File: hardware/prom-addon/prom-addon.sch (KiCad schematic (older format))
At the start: 5 parts

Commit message: The ROM reader addon schematic finished.
We are pretty much ready for layout. Status as of @esden twitch stream
on 2020-09-01.
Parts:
- removed U? (x2): 74HC164, symbol 74xx:74HC164
- added JP1, JP2: Pin Mode, Connector_PinHeader_2.54mm:PinHeader_1x03_P2.54mm_Vertical, symbol Jumper:Jumper_3_Bridged12
- added RN1, RN2, RN3: 100R, Resistor_SMD:R_Array_Convex_4x0402, symbol Device:R_Pack04
- added U1, U2: 74HC595, pkl_housings_dfn_qfn:DHVQFN-16_2.5x3.5mm_Pitch0.5mm, symbol 74xx:74HC595
- J1, J2: renamed from J?; footprint (none) -> Connector_PinSocket_2.54mm:PinSocket_2x10_P2.54mm_Vertical
- gave numbers to parts that had none: 1
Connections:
- net labels added: A_LATCH, A_SI´, P1, P27, ~OE
- wire segments 116 -> 137
- no-connect marks 10 -> 9
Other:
- note added: "Can be\nVpp or A15"
- note added: "Can be\n~PGM~ or A14"
- note added: "TODO:"
- note removed: "TODO:\n* Figure out if A15/PGM/VPP need jumpers\n* Figure out if the sift registers need to be different\n* Jumpering/padding for CE vs Address lines"
- moved on the sheet: J1, J2, U3

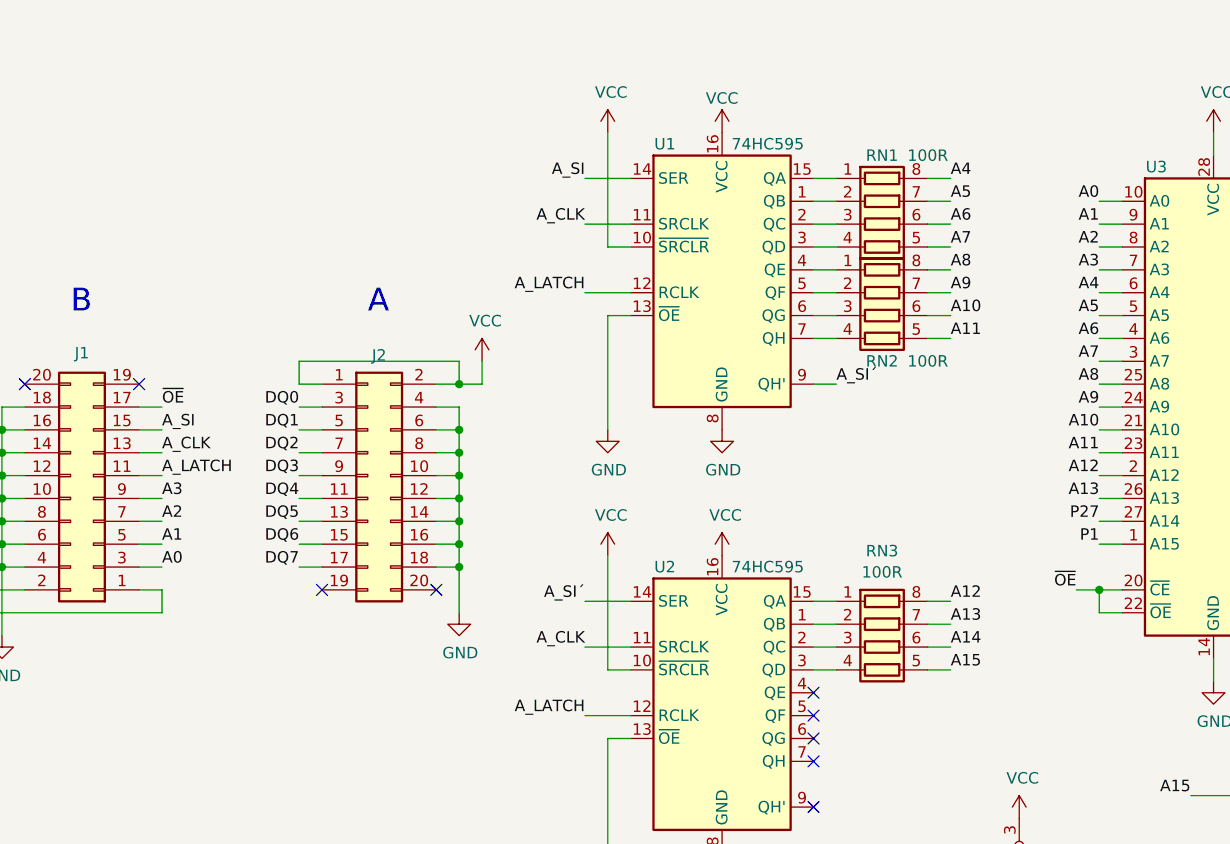
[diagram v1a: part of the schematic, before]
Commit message: prom: Routed the first version of the board.
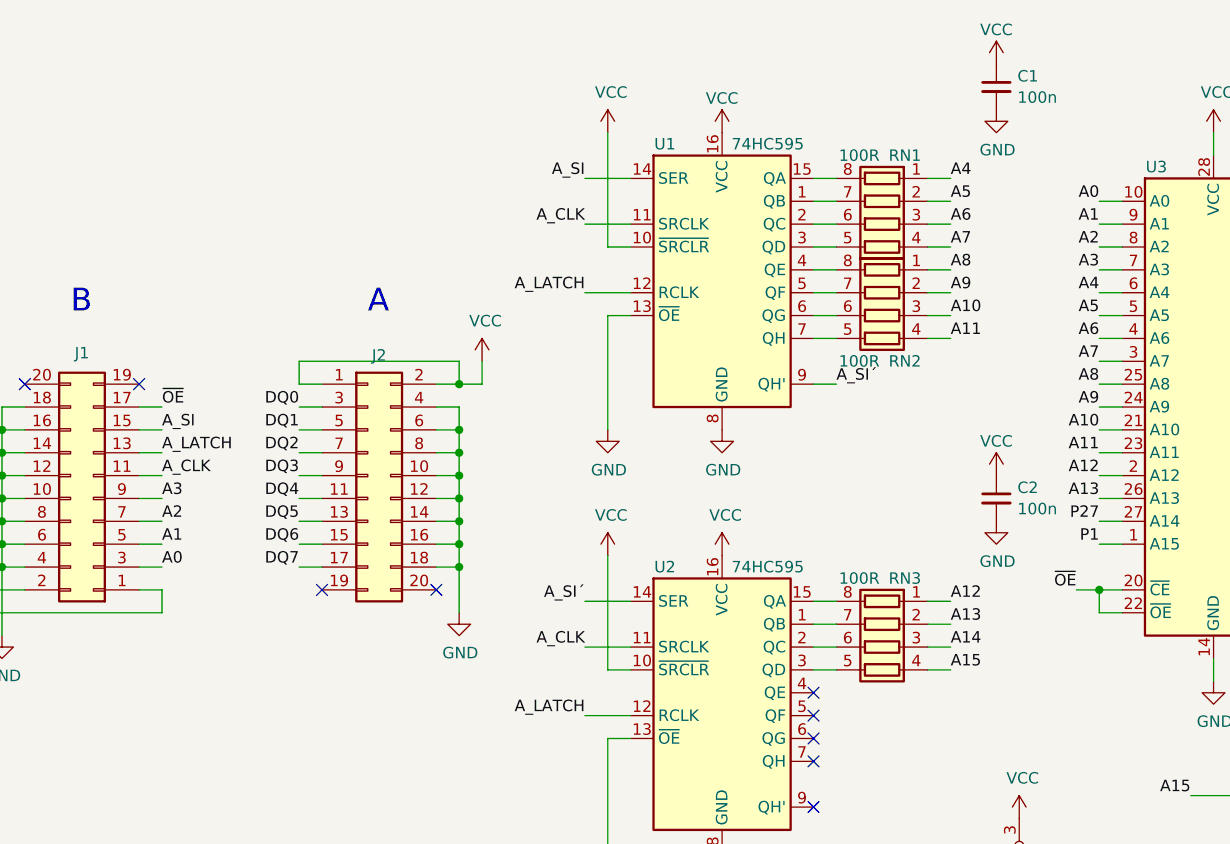
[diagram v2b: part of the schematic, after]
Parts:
- added C1, C2: 100n, pkl_dipol:C_0402, symbol Device:C_Small
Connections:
- net A10: now also RN2.3 (R3.1); no longer RN2.6 (R3.2)
- net A11: now also RN2.4 (R4.1); no longer RN2.5 (R4.2)
- net A12: now also RN3.1 (R1.1); no longer RN3.8 (R1.2)
- net A13: now also RN3.2 (R2.1); no longer RN3.7 (R2.2)
- net A14: now also RN3.3 (R3.1); no longer RN3.6 (R3.2)
- net A15: now also RN3.4 (R4.1); no longer RN3.5 (R4.2)
- net A4: now also RN1.1 (R1.1); no longer RN1.8 (R1.2)
- net A5: now also RN1.2 (R2.1); no longer RN1.7 (R2.2)
- net A6: now also RN1.3 (R3.1); no longer RN1.6 (R3.2)
- net A7: now also RN1.4 (R4.1); no longer RN1.5 (R4.2)
- net A8: now also RN2.1 (R1.1); no longer RN2.8 (R1.2)
- net A9: now also RN2.2 (R2.1); no longer RN2.7 (R2.2)
- net A_CLK: now also J1.11 (Pin_11); no longer J1.13 (Pin_13)
- net A_LATCH: now also J1.13 (Pin_13); no longer J1.11 (Pin_11)
- net GND: now also C1.2, C2.2
- net VCC: now also C1.1, C2.1
- net at U1.15 (QA): now also RN1.8 (R1.2); no longer RN1.1 (R1.1)
- net at U1.1 (QB): now also RN1.7 (R2.2); no longer RN1.2 (R2.1)
- net at U1.2 (QC): now also RN1.6 (R3.2); no longer RN1.3 (R3.1)
- net at U1.3 (QD): now also RN1.5 (R4.2); no longer RN1.4 (R4.1)
- net at U1.4 (QE): now also RN2.8 (R1.2); no longer RN2.1 (R1.1)
- net at U1.5 (QF): now also RN2.7 (R2.2); no longer RN2.2 (R2.1)
- net at U1.6 (QG): now also RN2.6 (R3.2); no longer RN2.3 (R3.1)
- net at U1.7 (QH): now also RN2.5 (R4.2); no longer RN2.4 (R4.1)
- net at U2.15 (QA): now also RN3.8 (R1.2); no longer RN3.1 (R1.1)
- net at U2.1 (QB): now also RN3.7 (R2.2); no longer RN3.2 (R2.1)
- net at U2.2 (QC): now also RN3.6 (R3.2); no longer RN3.3 (R3.1)
- net at U2.3 (QD): now also RN3.5 (R4.2); no longer RN3.4 (R4.1)
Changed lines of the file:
@@
 Text Label 2500 2300 0    50   ~ 0
 A_SI
-Text Label 2500 2400 0    50   ~ 0
+Text Label 2500 2500 0    50   ~ 0
 A_CLK
 Text Label 2500 2900 0    50   ~ 0
@@
 	6600 3000 6500 3000
 Connection ~ 6600 3000
-Text Label 2500 2500 0    50   ~ 0
+Text Label 2500 2400 0    50   ~ 0
 A_LATCH
 Text Label 2500 2200 0    50   ~ 0
@@
 U 1 1 5F57774C
 P 5650 1400
-F 0 "RN1" V 5350 1400 50  0000 C CNN
-F 1 "100R" V 5350 1600 50  0000 C CNN
+F 0 "RN1" V 5350 1300 50  0000 C CNN
+F 1 "100R" V 5350 1500 50  0000 C CNN
 F 2 "Resistor_SMD:R_Array_Convex_4x0402" V 5925 1400 50  0001 C CNN
 F 3 "~" H 5650 1400 50  0001 C CNN
 	1    5650 1400
-	0    1    1    0
+	0    -1   1    0
 $EndComp
 $Comp
@@
 U 1 1 5F581391
 P 5650 1800
-F 0 "RN2" V 5850 1800 50  0000 C CNN
-F 1 "100R" V 5850 2000 50  0000 C CNN
+F 0 "RN2" V 5850 1700 50  0000 C CNN
+F 1 "100R" V 5850 1900 50  0000 C CNN
 F 2 "Resistor_SMD:R_Array_Convex_4x0402" V 5925 1800 50  0001 C CNN
 F 3 "~" H 5650 1800 50  0001 C CNN
 	1    5650 1800
-	0    1    1    0
+	0    -1   1    0
 $EndComp
 Wire Wire Line
@@
 U 1 1 5F5B0FC8
 P 5650 3250
-F 0 "RN3" V 5230 3250 50  0000 C CNN
-F 1 "100R" V 5323 3250 50  0000 C CNN
+F 0 "RN3" V 5350 3150 50  0000 C CNN
+F 1 "100R" V 5350 3350 50  0000 C CNN
 F 2 "Resistor_SMD:R_Array_Convex_4x0402" V 5925 3250 50  0001 C CNN
 F 3 "~" H 5650 3250 50  0001 C CNN
 	1    5650 3250
-	0    1    1    0
+	0    -1   1    0
 $EndComp
 Wire Wire Line
@@
 Wire Wire Line
 	6600 2800 6700 2800
+$Comp
+L Device:C_Small C2
+U 1 1 5F744BFD
+P 6150 2600
+F 0 "C2" H 6242 2647 50  0000 L CNN
+F 1 "100n" H 6242 2554 50  0000 L CNN
+F 2 "pkl_dipol:C_0402" H 6150 2600 50  0001 C CNN
+F 3 "~" H 6150 2600 50  0001 C CNN
+	1    6150 2600
+	1    0    0    -1
+$EndComp
+$Comp
+L Device:C_Small C1
+U 1 1 5F745589
+P 6150 800
+F 0 "C1" H 6242 847 50  0000 L CNN
+F 1 "100n" H 6242 754 50  0000 L CNN
+F 2 "pkl_dipol:C_0402" H 6150 800 50  0001 C CNN
+F 3 "~" H 6150 800 50  0001 C CNN
+	1    6150 800
+	1    0    0    -1
+$EndComp
+$Comp
+L power:GND #PWR0117
+U 1 1 5F745B98
+P 6150 900
+F 0 "#PWR0117" H 6150 650 50  0001 C CNN
+F 1 "GND" H 6155 724 50  0000 C CNN
+F 2 "" H 6150 900 50  0001 C CNN
+F 3 "" H 6150 900 50  0001 C CNN
+	1    6150 900
+	1    0    0    -1
+$EndComp
+$Comp
+L power:VCC #PWR0118
+U 1 1 5F74C028
+P 6150 700
+F 0 "#PWR0118" H 6150 550 50  0001 C CNN
+F 1 "VCC" H 6150 850 50  0000 C CNN
+F 2 "" H 6150 700 50  0001 C CNN
+F 3 "" H 6150 700 50  0001 C CNN
+	1    6150 700
+	1    0    0    -1
+$EndComp
+$Comp
+L power:VCC #PWR0119
+U 1 1 5F759CD8
+P 6150 2500
+F 0 "#PWR0119" H 6150 2350 50  0001 C CNN
+F 1 "VCC" H 6150 2650 50  0000 C CNN
+F 2 "" H 6150 2500 50  0001 C CNN
+F 3 "" H 6150 2500 50  0001 C CNN
+	1    6150 2500
+	1    0    0    -1
+$EndComp
+$Comp
+L power:GND #PWR0120
+U 1 1 5F759F0D
+P 6150 2700
+F 0 "#PWR0120" H 6150 2450 50  0001 C CNN
+F 1 "GND" H 6155 2524 50  0000 C CNN
+F 2 "" H 6150 2700 50  0001 C CNN
+F 3 "" H 6150 2700 50  0001 C CNN
+	1    6150 2700
+	1    0    0    -1
+$EndComp
 $EndSCHEMATC

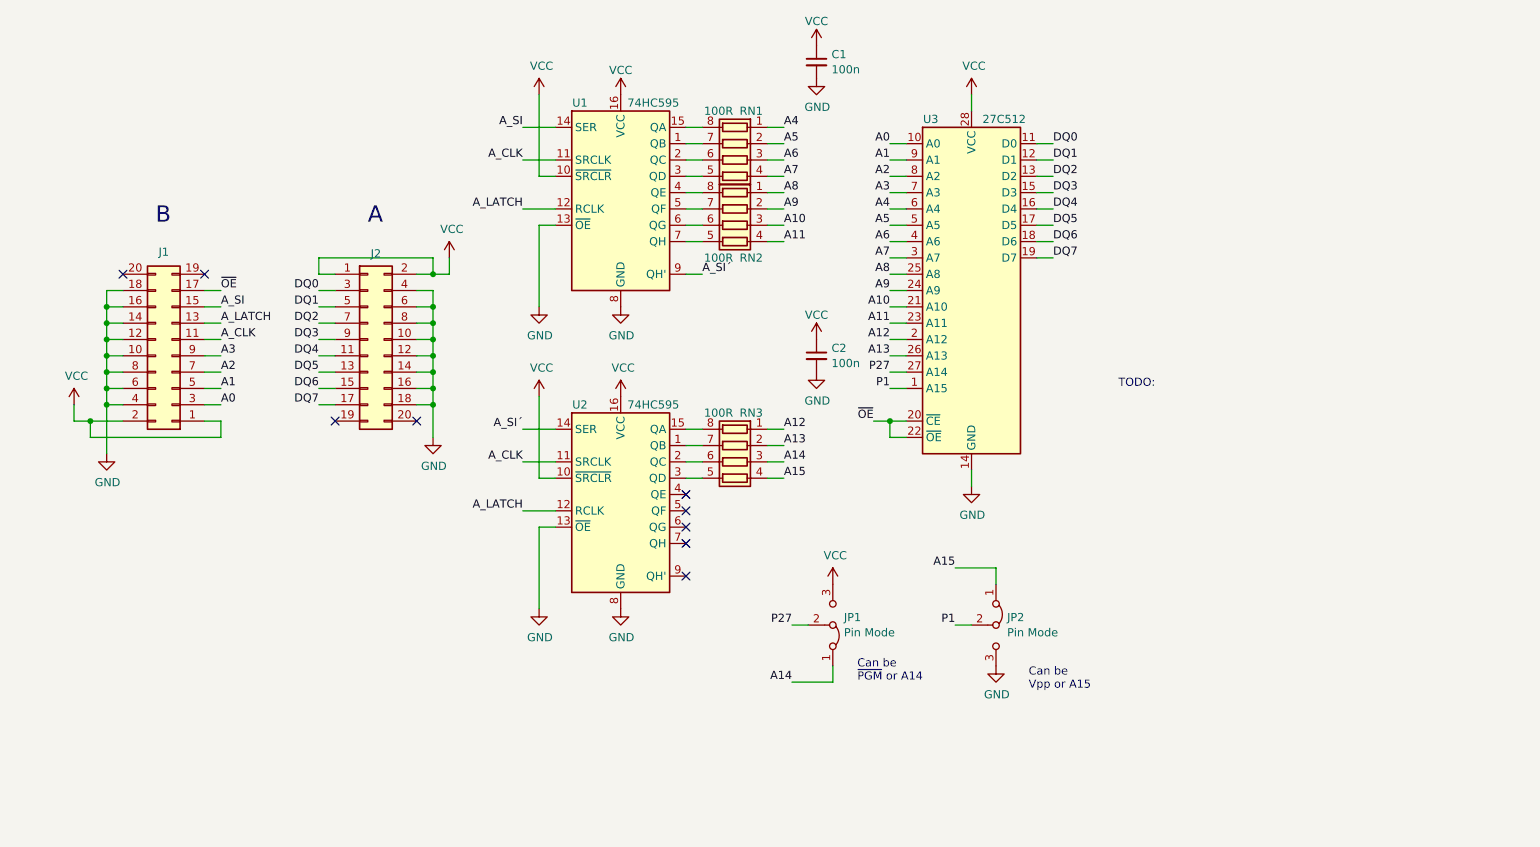
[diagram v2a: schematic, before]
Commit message: Replaced supply fills with point to point routing.
Will look better in afterdark. ;)
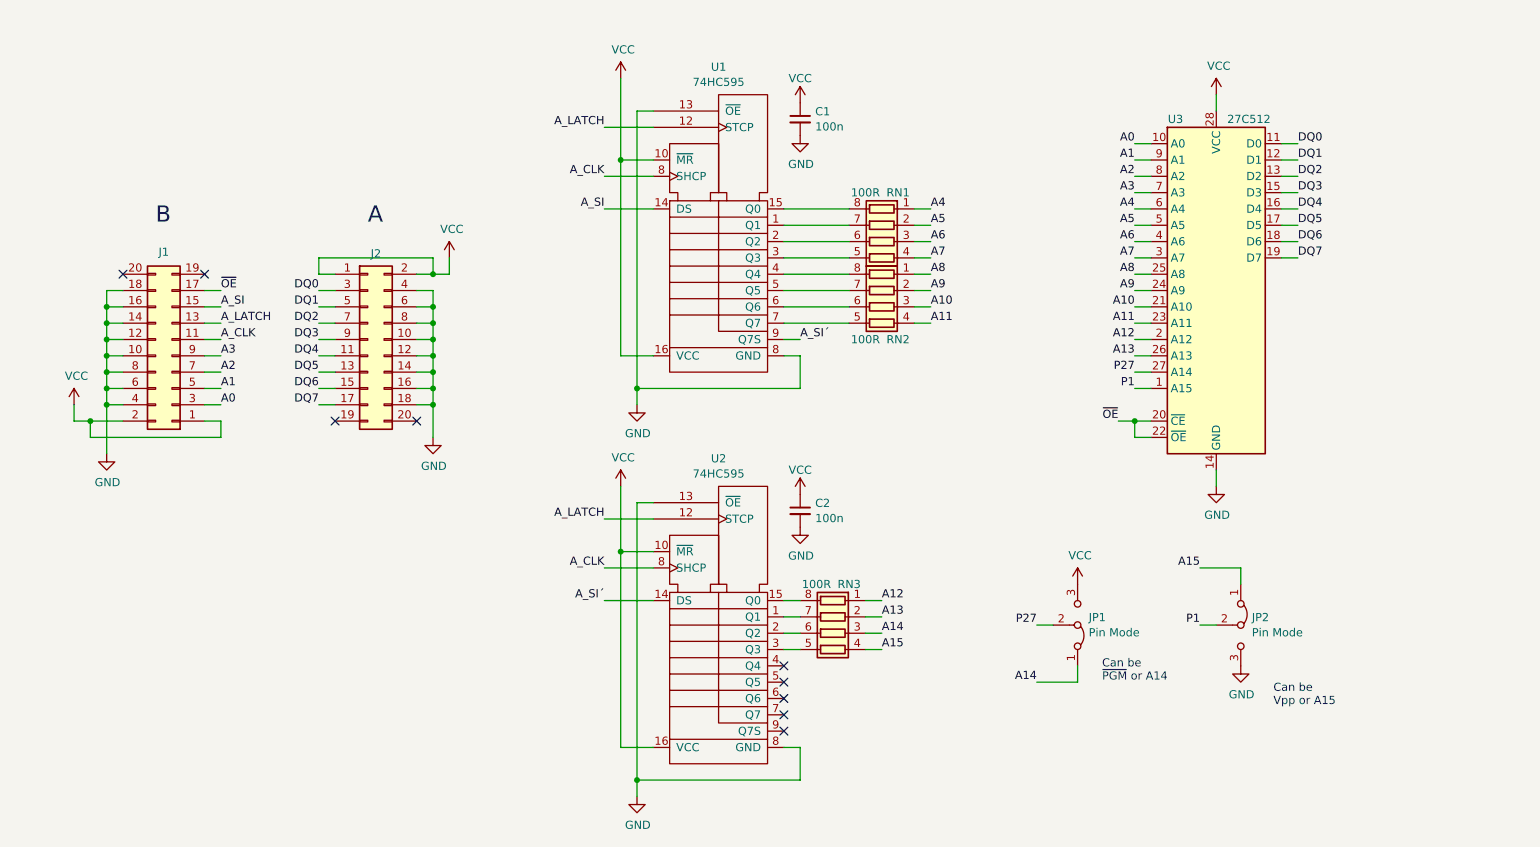
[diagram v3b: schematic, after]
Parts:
- removed U1, U2: 74HC595, pkl_housings_dfn_qfn:DHVQFN-16_2.5x3.5mm_Pitch0.5mm, symbol 74xx:74HC595
- added U1, U2: 74HC595, pkl_housings_dfn_qfn:DHVQFN-16_2.5x3.5mm_Pitch0.5mm, symbol pkl_misc:74HC595
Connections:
- net A_CLK: now also U1.8 (SHCP), U2.8 (SHCP)
- net A_LATCH: now also U1.12 (STCP), U2.12 (STCP)
- net A_SI: now also U1.14 (DS)
- net A_SI´: now also U1.9 (Q7S), U2.14 (DS)
- net GND: now also U1.13 (~OE), U1.17 (PAD), U1.8 (SHCP), U2.13 (~OE), U2.17 (PAD), U2.8 (SHCP)
- net VCC: now also U1.10 (~MR), U1.16 (VCC), U2.10 (~MR), U2.16 (VCC)
- net at RN1.5 (R4.2): now also U1.3 (Q3)
- net at RN1.6 (R3.2): now also U1.2 (Q2)
- net at RN1.7 (R2.2): now also U1.1 (Q1)
- net at RN1.8 (R1.2): now also U1.15 (Q0)
- net at RN2.5 (R4.2): now also U1.7 (Q7)
- net at RN2.6 (R3.2): now also U1.6 (Q6)
- net at RN2.7 (R2.2): now also U1.5 (Q5)
- net at RN2.8 (R1.2): now also U1.4 (Q4)
- net at RN3.5 (R4.2): now also U2.3 (Q3)
- net at RN3.6 (R3.2): now also U2.2 (Q2)
- net at RN3.7 (R2.2): now also U2.1 (Q1)
- net at RN3.8 (R1.2): now also U2.15 (Q0)
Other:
- note removed: "TODO:"
- moved on the sheet: C1, C2, JP1, JP2, RN1, RN2, RN3, U3

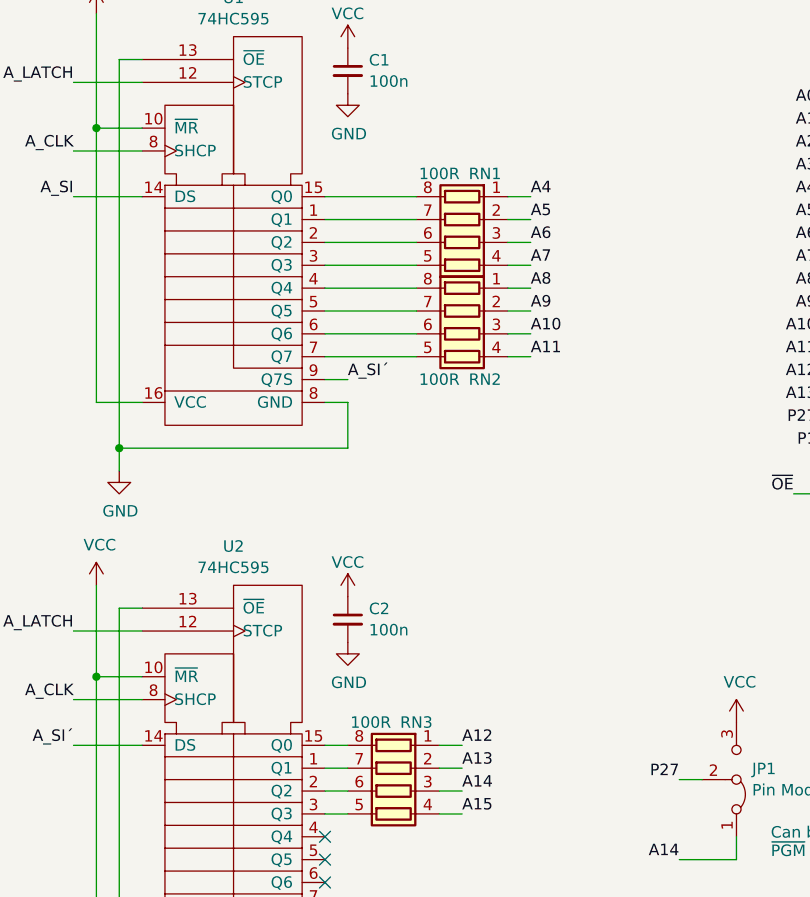
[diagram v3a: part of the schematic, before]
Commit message: prom: Added silkscreen legend. Bumped version.
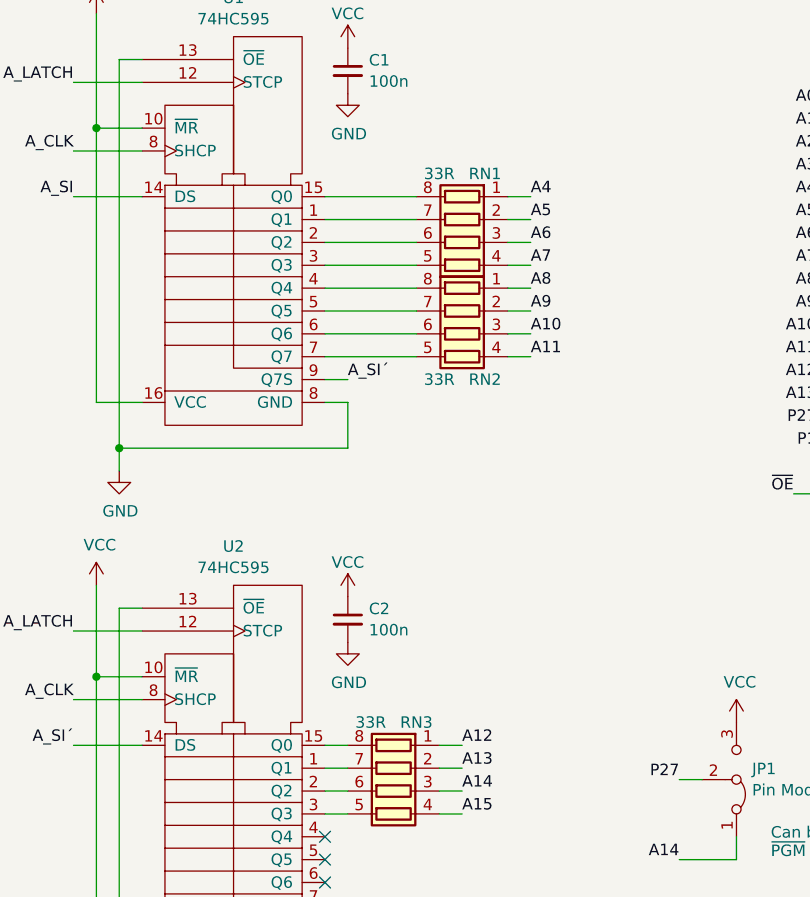
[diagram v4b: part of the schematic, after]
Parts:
- RN1, RN2, RN3: value 100R -> 33R
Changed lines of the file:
@@
 Title "Glasgow PROM Interface Addon"
 Date ""
-Rev ""
+Rev "V1.0a"
 Comp "1BitSquared"
-Comment1 "(C) 2020 Piotr Esden-Tempski <piotr@esden.net>"
-Comment2 "(C) 2020 1BitSquared <info@1bitsquared.com>"
+Comment1 "(C) 2020-2021 Piotr Esden-Tempski <piotr@esden.net>"
+Comment2 "(C) 2020-2021 1BitSquared <info@1bitsquared.com>"
 Comment3 "License: CC-BY-SA 4.0"
 Comment4 ""
@@
 P 6550 1900
 F 0 "RN1" V 6250 1800 50  0000 C CNN
-F 1 "100R" V 6250 2000 50  0000 C CNN
+F 1 "33R" V 6250 2000 50  0000 C CNN
 F 2 "Resistor_SMD:R_Array_Convex_4x0402" V 6825 1900 50  0001 C CNN
 F 3 "~" H 6550 1900 50  0001 C CNN
@@
 P 6550 2300
 F 0 "RN2" V 6750 2200 50  0000 C CNN
-F 1 "100R" V 6750 2400 50  0000 C CNN
+F 1 "33R" V 6750 2400 50  0000 C CNN
 F 2 "Resistor_SMD:R_Array_Convex_4x0402" V 6825 2300 50  0001 C CNN
 F 3 "~" H 6550 2300 50  0001 C CNN
@@
 P 6250 4300
 F 0 "RN3" V 5950 4200 50  0000 C CNN
-F 1 "100R" V 5950 4400 50  0000 C CNN
+F 1 "33R" V 5950 4400 50  0000 C CNN
 F 2 "Resistor_SMD:R_Array_Convex_4x0402" V 6525 4300 50  0001 C CNN
 F 3 "~" H 6250 4300 50  0001 C CNN
